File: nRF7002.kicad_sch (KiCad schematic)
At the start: 8 parts, among them U1 nRF7002-QFXX, U9 TPS22917DBV, Y1 40 MHz

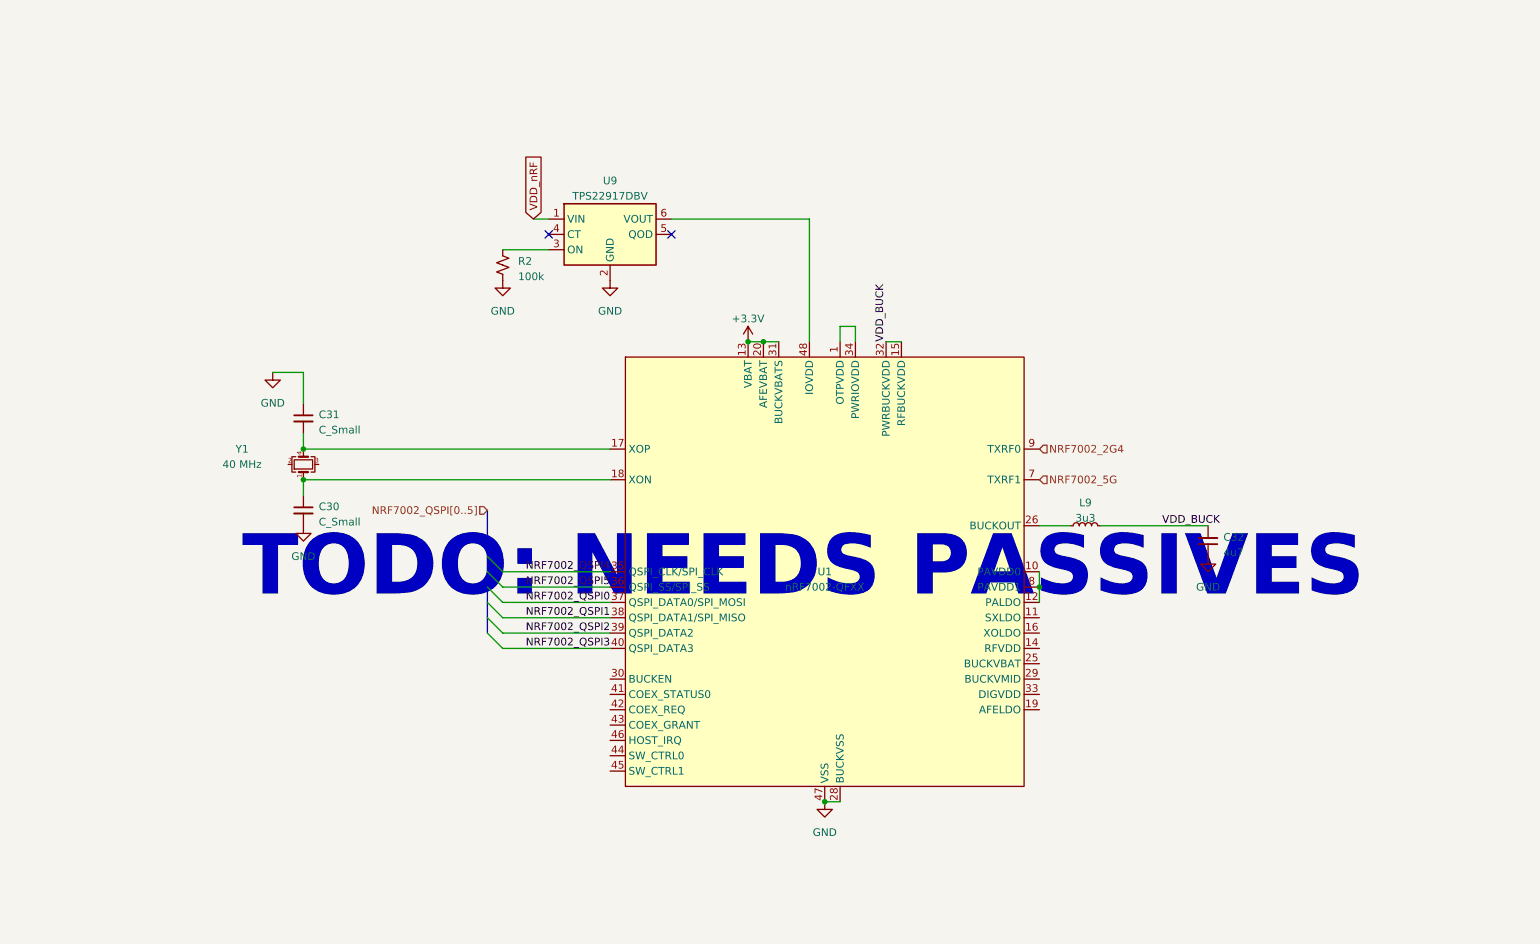
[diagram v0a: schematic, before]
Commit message: Added passvies and bus connections to nRF7002
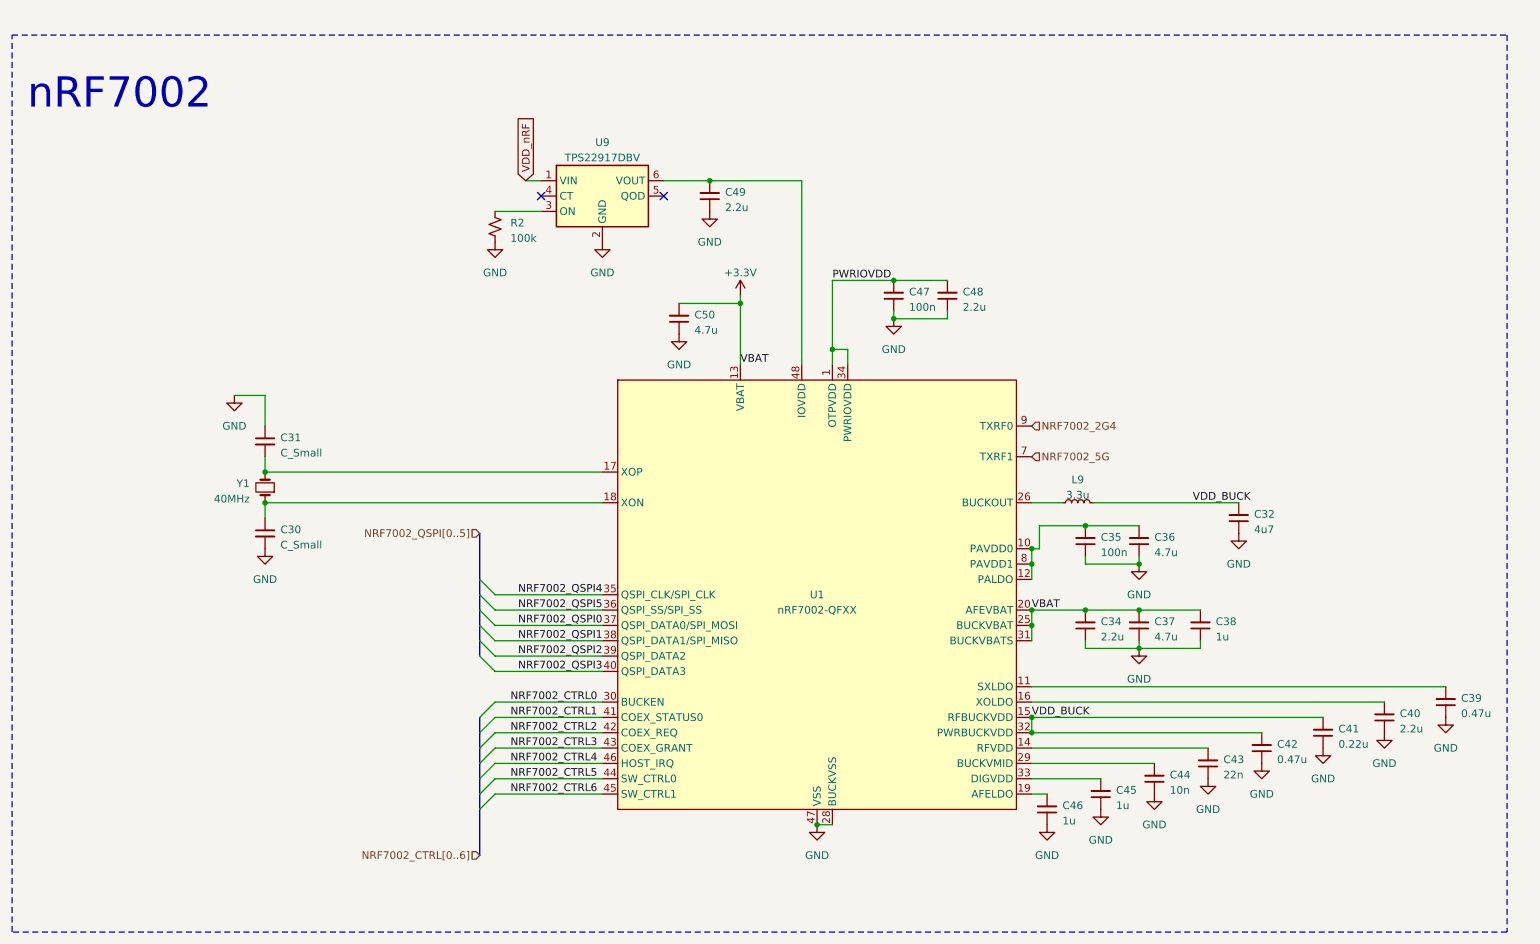
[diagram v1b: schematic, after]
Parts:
- removed Y1: 40 MHz, symbol Device:Crystal_GND23_Small
- added C34, C40, C48, C49: 2.2u, symbol Device:C_Small
- added C35, C47: 100n, symbol Device:C_Small
- added C36, C37, C50: 4.7u, symbol Device:C_Small
- added C38, C45, C46: 1u, symbol Device:C_Small
- added C39, C42: 0.47u, symbol Device:C_Small
- added C41: 0.22u, symbol Device:C_Small
- added C43: 22n, symbol Device:C_Small
- added C44: 10n, symbol Device:C_Small
- added Y1: 40MHz, symbol Device:Crystal_Small
- L9: value 3u3 -> 3.3u
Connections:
- net +3.3V: now also U1.25 (BUCKVBAT), C34.2, C37.2, C38.2, C50.2
- net GND: now also C34.1, C35.1, C36.1, C37.1, C38.1, C39.1, C40.1, C41.1, C42.1, C43.1, C44.1, C45.1, C46.1, C47.1, C48.1, C49.1, C50.1
- net VDD_BUCK: now also C41.2, C42.2
- net at C30.1, U1.18 (XON): now also Y1.1
- net PWRIOVDD: now reaches U1.1 (OTPVDD), U1.34 (PWRIOVDD)
- net PWRIOVDD: now also C47.2, C48.2
- net at U1.10 (PAVDD0), U1.12 (PALDO), U1.8 (PAVDD1): now also C35.2, C36.2
- net at U1.11 (SXLDO): now also C39.2
- net at U1.14 (RFVDD): now also C43.2
- net at U1.16 (XOLDO): now also C40.2
- net at C31.2, U1.17 (XOP): now also Y1.2
- net at U1.19 (AFELDO): now also C46.2
- net at U1.29 (BUCKVMID): now also C44.2
- net NRF7002_CTRL0: now reaches U1.30 (BUCKEN)
- net at U1.33 (DIGVDD): now also C45.2
- net NRF7002_CTRL1: now reaches U1.41 (COEX_STATUS0)
- net NRF7002_CTRL2: now reaches U1.42 (COEX_REQ)
- net NRF7002_CTRL3: now reaches U1.43 (COEX_GRANT)
- net NRF7002_CTRL5: now reaches U1.44 (SW_CTRL0)
- net NRF7002_CTRL6: now reaches U1.45 (SW_CTRL1)
- net NRF7002_CTRL4: now reaches U1.46 (HOST_IRQ)
- net at U1.48 (IOVDD), U9.6 (VOUT): now also C49.2
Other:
- note added: "nRF7002"
- note removed: "TODO: NEEDS PASSIVES"
- moved on the sheet: C30, C31, R2, U1, U9

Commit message: Schematic complete.
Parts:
- removed C49: 2.2u, symbol Device:C_Small
- removed R2: 100k, symbol Device:R_Small_US
- removed U9: TPS22917DBV, Package_TO_SOT_SMD:SOT-23-6, symbol Power_Management:TPS22917DBV
- C30, C31: value C_Small -> 12p; footprint (none) -> Capacitor_SMD:C_0201_0603Metric
- C32: value 4u7 -> 4.7u; footprint (none) -> Capacitor_SMD:C_0402_1005Metric
- C34, C36, C37, C38, C40, C45, C46, C48, C50: footprint (none) -> Capacitor_SMD:C_0402_1005Metric
- C35, C39, C41, C42, C43, C44, C47: footprint (none) -> Capacitor_SMD:C_0201_0603Metric
- L9: footprint (none) -> Inductor_SMD:L_0603_1608Metric
- Y1: footprint (none) -> Crystal:Crystal_SMD_2016-4Pin_2.0x1.6mm; symbol Device:Crystal_Small -> Device:Crystal_GND24_Small; MPN (none) -> XRCGB40M000F1S1BR0
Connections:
- net GND: now also Y1.2, Y1.4
- net at C31.2, U1.17 (XOP): now also Y1.3; no longer Y1.2
- net IOVDD_IN: now reaches U1.48 (IOVDD)
- net +3.3V renamed +3V3
- no-connect marks 2 -> 0
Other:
- moved on the sheet: C30, C31, C32, C34, C35, C36, C37, C38, C39, C40, C41, C42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
